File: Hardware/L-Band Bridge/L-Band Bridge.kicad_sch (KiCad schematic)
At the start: 0 parts

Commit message: Updating L-Band Bridge Schematic
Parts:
- added C1, C2: 100pF, symbol Device:C_Small
- added C3: 100nF, symbol Device:C_Small
- added J1, J2: SMA, symbol Connector:Conn_Coaxial
- added L1: 220nH, symbol Device:L_Small
- added R1: 8.25, symbol Device:R_Small_US
- added R2: 143, symbol Device:R_Small_US
- added U1: ADP-2-20+, RF_Mini-Circuits:Mini-Circuits_CD636_LandPatternPL-035, symbol _tim-RF:ADP-2-20+
- added U2, U3: ADL5904, Package_CSP:LFCSP-16-1EP_3x3mm_P0.5mm_EP1.6x1.6mm, symbol RF:ADL5904
- added U4, U5: GALI-52, Package_TO_SOT_SMD:SOT-89-3, symbol RF_Amplifier:GALI-52
- added U6: HMC472ALP4E, symbol _tim-RF:HMC472ALP4E
- added U7: ADE-17H+, RF_Mini-Circuits:Mini-Circuits_CD542_LandPatternPL-052, symbol _tim-RF:ADE-17H+
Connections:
- new net: U3.11 (GND), U3.17 (GND)
- new net: U3.5 (VPOS), U3.7 (VPOS)
- new net: U7.1 (GND), U7.4 (GND), U7.5 (GND)
- new net: U2.11 (GND), U2.17 (GND)
- new net: U2.5 (VPOS), U2.7 (VPOS)
- new net GND: J1.2 (Ext), U1.6 (GND), U6.1 (GND), U6.12 (GND), U6.14 (GND), U6.16 (GND), U6.17 (GND), U6.18 (GND), U6.25 (GND), U6.3 (GND), U6.5 (GND)
- new net RF_IN: J1.1 (In), U1.1 (SUM)
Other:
- note added: "ADE-17H+ Mixer (MOUSER)"
- note added: "ADP-2-20+ Power Divider"
- note added: "GALI-52+ AMP"
- note added: "HMC472ALP4 6-bit digital control attenuator"
- note added: "MAPS-010163-TR0500 1.4-2.4 GHz Phase Shifter"

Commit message: Updates to L-Band Bridge
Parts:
- removed U2, U3: ADL5904, Package_CSP:LFCSP-16-1EP_3x3mm_P0.5mm_EP1.6x1.6mm, symbol RF:ADL5904
- added C10, C11, C8, C9: 330pF, symbol Device:C_Small
- added C12, C13, C14, C4, C5: 100pF, symbol Device:C_Small
- added C15, C16, C20, C6, C7: 100nF, symbol Device:C_Small
- added C18, C19: 10nF, symbol Device:C_Small
- added J3: SMA, symbol Connector:Conn_Coaxial
- added L2: 220nH, symbol Device:L_Small
- added R3: 143, symbol Device:R_Small_US
- added R4: 8.25, symbol Device:R_Small_US
- added R5: 60.4, symbol Device:R_Small_US
- added R6: 2k, symbol Device:R_Small_US
- added R7: 3.74k, symbol Device:R_Small_US
- added R8: 1.5k, symbol Device:R_Small_US
- added R9: 270, symbol Device:R_Small_US
- added U10, U9: DBTC-17-5LX+, symbol _tim-RF:DBTC-17-5LX+
- added U2: ~, symbol _tim-RF:ADL5906
- added U8: ~, symbol _tim-RF:MAPS-010163-TR0500
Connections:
- net +12V: now also C3.2, R1.2, C6.2, R4.1
- net GND: now also C3.1, J2.2 (Ext), U4.2 (GND), U5.2 (GND), U7.1 (GND), U7.4 (GND), U7.5 (GND), C10.1, C11.1, C13.1, C14.2, C15.2, C16.1, C19.2, C20.2, C6.1, C7.2, C8.1, C9.1, J3.2 (Ext), R5.1, R6.1, R9.2, U10.2 (GND), U2.17 (GND), U2.4 (GND), U2.9 (GND), U8.10 (GND), U8.11 (GND), U8.12 (GND), U8.13 (GND), U8.15 (GND), U8.16 (GND), U8.2 (P/S), U8.25 (GND), U8.3 (GND), U8.4 (GND), U8.6 (GND), U8.7 (GND), U8.8 (GND), U8.9 (GND), U9.2 (GND)
- net at R1.1: now also R2.1
- net at U7.3 (RF): now also U10.4 (OUT)
- net at U7.6 (LO): now also C5.2
- net at U4.1: now also C1.2
- net at U4.3: now also C2.1, L1.2
- net at U6.10 (ACG5): now also C9.2
- net at U6.11 (ACG6): now also C10.2
- net at U6.13 (ACG7): now also C11.2
- net at U6.15 (RF2): now also C1.1
- net ATTEN_D0: now reaches U6.19 (V1)
- net +5V: now reaches U6.2 (Vdd)
- net +5V: now also C13.2, C14.1, C15.1, C16.2, C7.1, U2.10 (VPOS2), U2.3 (VPOS1), U8.18 (VCC)
- net ATTEN_D1: now reaches U6.20 (V2)
- net ATTEN_D2: now reaches U6.21 (V3)
- net ATTEN_D3: now reaches U6.22 (V4)
- net ATTEN_D4: now reaches U6.23 (V5)
- net ATTEN_D5: now reaches U6.24 (V6)
- net at U6.4 (RF1): now also C12.2
- net at U6.6 (ACG1): now also U6.7 (ACG2), U6.8 (ACG3), U6.9 (ACG4), C8.2
- net at L1.1: now also R2.2
- net at U5.1: now also C4.2
- net at U5.3: now also C5.1, L2.1
- net at U1.3 (PORT1): now also C12.1
- net at U1.4 (PORT2): now also U8.5 (RF_IN)
- net TX_OUT: now reaches J2.1 (In)
- net TX_OUT: now also U9.4 (OUT)
- net at C2.2: now also U9.3 (IN)
- net RF_IN renamed SYNTH_IN
- new net: R7.1, R8.2, U2.11 (VREF)
- new net: R6.2, R7.2, U2.12 (VTGT)
- new net: C19.1, U2.15 (RFIN-)
- new net: C4.1, U8.14 (RF_OUT)
- new net: R8.1, R9.1, U2.1 (TADJ)
- new net: C20.1, U2.5 (CRMS)
- new net: C18.1, U2.14 (RFIN+)
- new net: R3.2, R4.2
- new net: U2.13 (NIC), U2.16 (NIC), U2.2 (NIC)
- new net: L2.2, R3.1
- new net -5V: U8.1 (VEE)
- new net PHASE_D0: U8.24 (D1_SER_IN)
- new net PHASE_D1: U8.23 (D2_CLK)
- new net PHASE_D2: U8.22 (D3_LE)
- new net PHASE_D3: U8.21 (D4)
- new net PHASE_D4: U8.20 (D5)
- new net PHASE_D5: U8.19 (D6)
- new net PHASE_SER_OUT: U8.17 (SER_OUT)
- new net RX_IN: J3.1 (In), U10.3 (IN)
- new net RX_MON: U10.1 (CPLD)
- new net TX_MON: C18.2, R5.2, U9.1 (CPLD)
- new net TX_MON_VOUT: U2.6 (VRMS), U2.7 (VSET)
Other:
- note added: "+12V Input"
- note added: "DC-DC Converter 12V to +5V and -5V RP-1205D OR PDQE10-Q24-D5-D"
- note added: "Directional Coupler DBTC-17-5LX+"
- note added: "L-Band Transmitter/Receiver"
- note added: "P/S LOW => Parallel Mode"
- moved on the sheet: C1, C2, C3, J1, J2, L1, R1, R2, U1, U4, U5, U6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

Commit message: Updates to L-Band Bridge
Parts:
- added C17, C21: 3.9nF, symbol Device:C_Small
- added C22: 6.8nF, symbol Device:C_Small
- added C23, C24, C25, C26, C27, C28, C31, C33, C34: 100nF, symbol Device:C_Small
- added C29, C30, C32, C35, C41: 100pF, symbol Device:C_Small
- added C36: 100uF, symbol Device:C_Polarized_Small
- added C37, C38: 10uF, symbol Device:C_Small
- added C39, C40: 330pF, symbol Device:C_Small
- added L3, L4: 10uH, symbol Device:L_Small
- added PS1: PDQE10-Q24-D5-D, symbol _tim-DC_DC:PDQE10-Q24-D5-D
- added Q1: MMBT3904, Package_TO_SOT_THT:TO-92_Inline, symbol Transistor_BJT:MMBT3904
- added R10: 82k, symbol Device:R_Small_US
- added R11, R12, R23: 10k, symbol Device:R_Small_US
- added R13: 220, symbol Device:R_Small_US
- added R14: 60.4, symbol Device:R_Small_US
- added R15, R24: 100k, symbol Device:R_Small_US
- added R16: 50, symbol Device:R_Small_US
- added R17, R22: 2k, symbol Device:R_Small_US
- added R18: 18k, symbol Device:R_Small_US
- added R19: 3.74k, symbol Device:R_Small_US
- added R20: 1.5k, symbol Device:R_Small_US
- added R21: 270, symbol Device:R_Small_US
- added U11: ~, symbol _tim-RF:ADL5906
- added U3: LM358, symbol Amplifier_Operational:LM358
- C18, C19: value 10nF -> 100pF
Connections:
- net +12V: now also C28.2, C36.1, PS1.2 (VIN), R10.1, R12.1, R24.1, U3.8 (V+)
- net +5V: now also C31.1, C32.2, C34.2, C35.1, C37.2, C40.2, PS1.3 (+VOUT), U11.10 (VPOS2), U11.3 (VPOS1)
- net -5V: now also C38.1, C39.1, PS1.5 (-VOUT)
- net GND: now also C18.2, C17.2, C21.2, C22.2, C24.1, C26.1, C28.1, C30.2, C31.2, C32.1, C33.2, C34.1, C35.2, C36.2, C37.1, C38.2, C39.2, C40.1, C41.1, PS1.1 (GND), PS1.4 (0V), R11.2, R13.2, R14.1, R15.2, R21.2, R22.1, U11.17 (GND), U11.4 (GND), U11.9 (GND), U3.4 (V-); no longer C19.2
- net RX_MON: now also C19.1, R14.2
- net TX_MON: now also C29.1; no longer C18.2
- net 2.3V: now reaches R7.1, R8.2, U2.11 (VREF)
- net 2.3V: now also R19.1, R20.2, U11.11 (VREF)
- net at U2.15 (RFIN-): now also C18.1; no longer C19.1
- net IF: now reaches U7.2 (IF)
- net IF: now also C17.1, L3.1
- net at U2.14 (RFIN+): now also C29.2; no longer C18.1
- new net: C41.2, R23.1, U3.5 (+)
- new net: C26.2, R17.1
- new net: C33.1, U11.5 (CRMS)
- new net: C23.2, Q1.1 (B), R10.2, R11.1
- new net: R16.1, U3.6 (-), U3.7
- new net: C22.1, L3.2, L4.1
- new net: R18.1, R23.2, U3.1
- new net: C25.2, R15.1, R24.2, U3.3 (+)
- new net: C24.2, Q1.2 (E), R13.1
- new net: C30.1, U11.15 (RFIN-)
- new net: C19.2, U11.14 (RFIN+)
- new net: R17.2, R18.2, U3.2 (-)
- new net: C27.1, R16.2
- new net: R19.2, R22.2, U11.12 (VTGT)
- new net: R20.1, R21.1, U11.1 (TADJ)
- new net: U11.13 (NIC), U11.16 (NIC), U11.2 (NIC)
- new net IF_AMP_OUT: C25.1, Q1.3 (C), R12.2
- new net IF_LPF_OUT: C21.1, C23.1, L4.2
- new net IF_OUT: C27.2
- new net RX_MON_VOUT: U11.6 (VRMS), U11.7 (VSET)
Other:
- note added: "0.35V VTADJ Recommended for 10 MHz to 2.14 GHz"
- moved on the sheet: C13, C14, C15, C16, C20, R5, R6, R7, R8, R9, U2

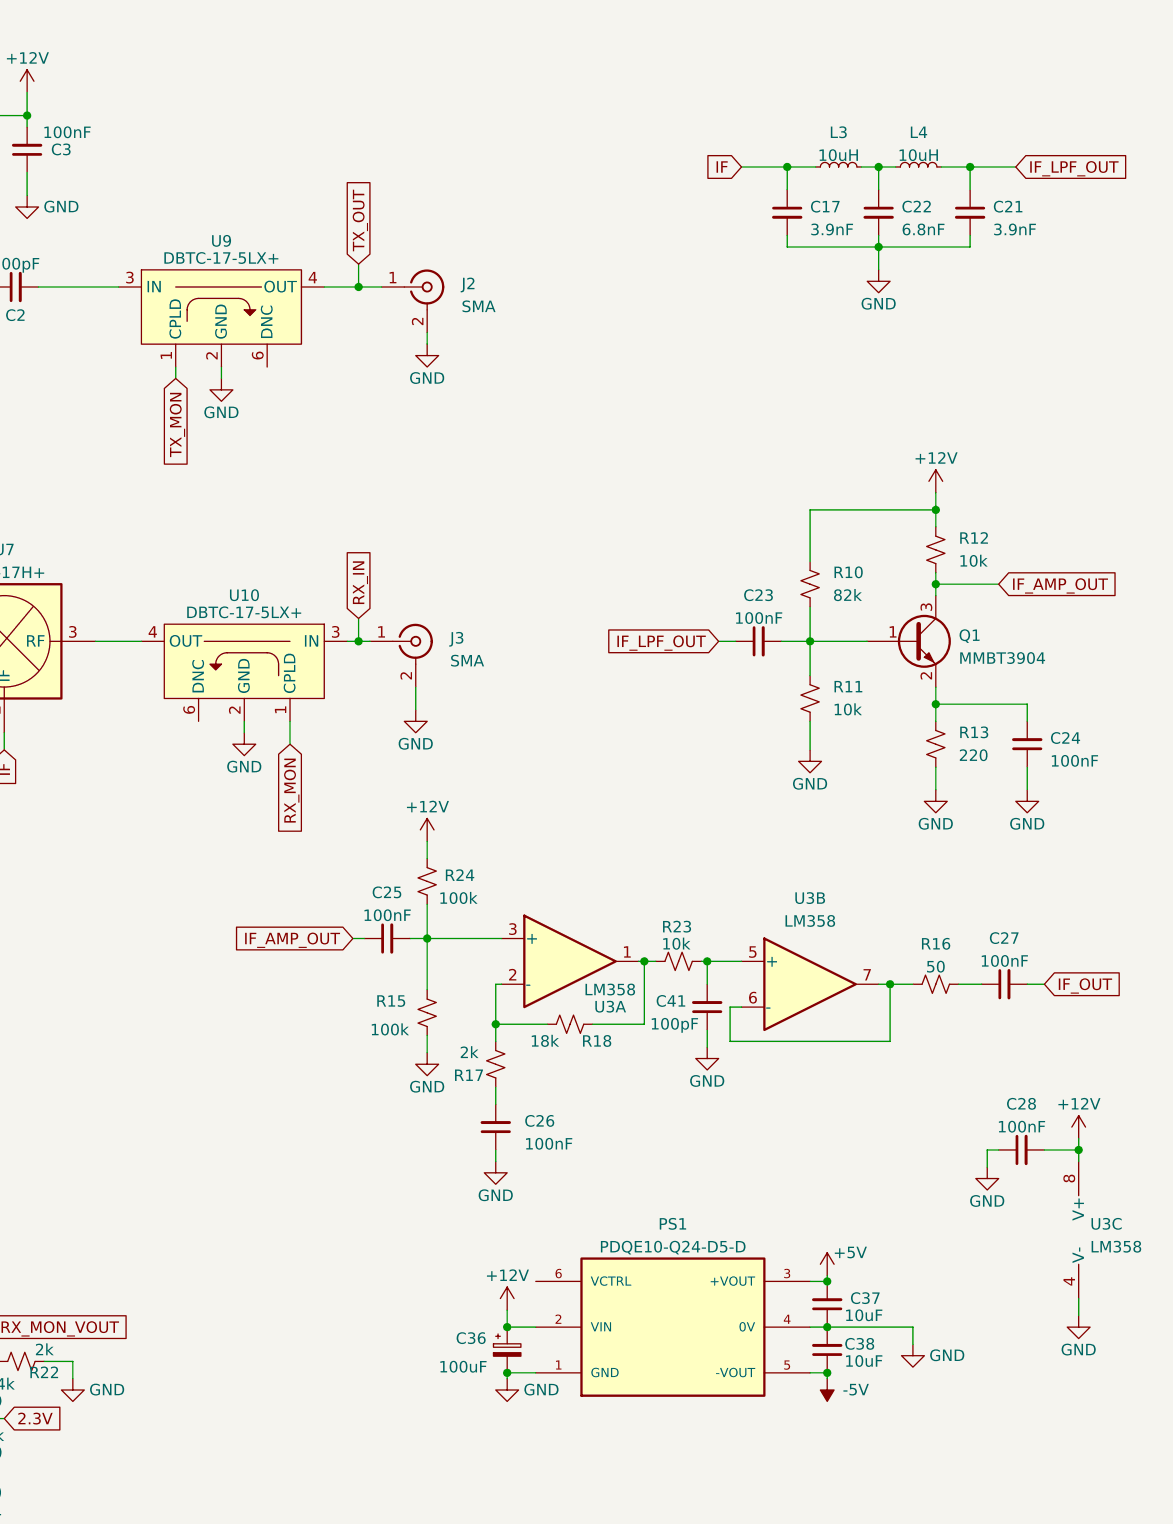
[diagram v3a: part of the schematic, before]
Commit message: L-Band Bridge Schematic Updates
Assigning footprints
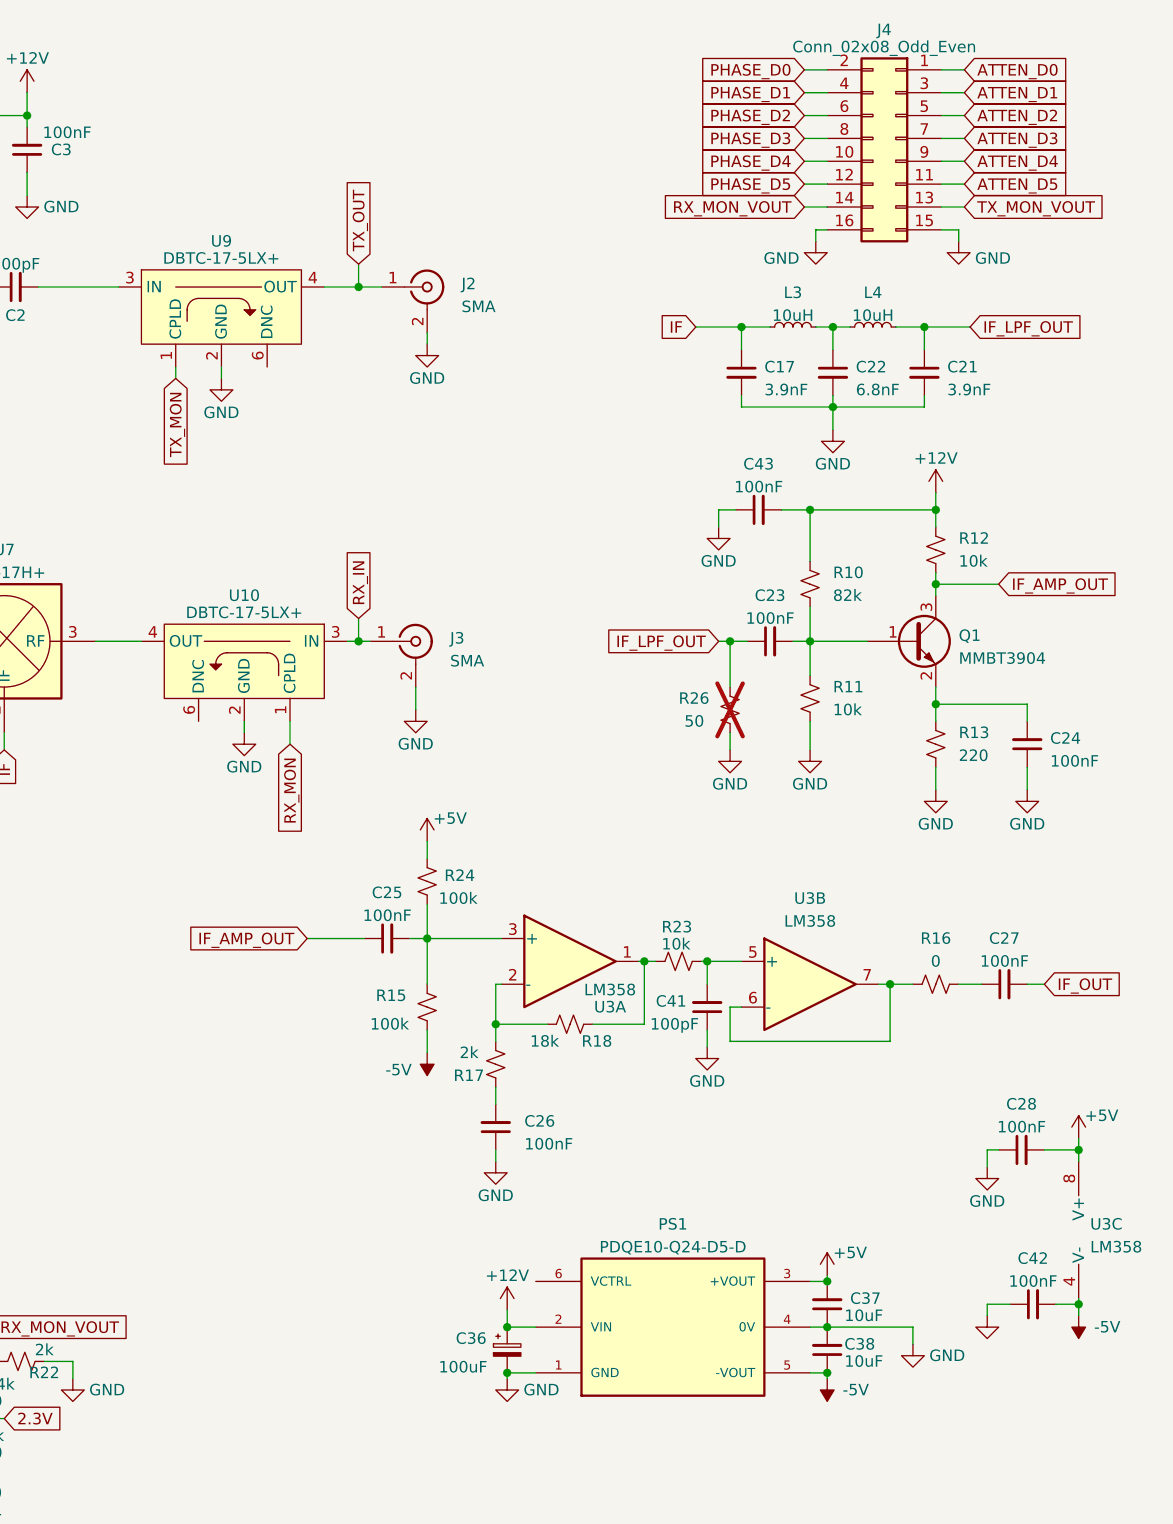
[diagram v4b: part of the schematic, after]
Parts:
- added C42, C43: 100nF, Capacitor_SMD:C_0402_1005Metric, symbol Device:C_Small
- added J4: Conn_02x08_Odd_Even, Connector_PinHeader_2.54mm:PinHeader_2x08_P2.54mm_Vertical, symbol Connector_Generic:Conn_02x08_Odd_Even
- added R26: 50, Capacitor_SMD:C_0603_1608Metric, symbol Device:R_Small_US
- C1, C10, C11, C12, C13, C14, C15, C16, C17, C18, C19, C2, C20, C21, C22, C23, C24, C25, C26, C27, C28, C29, C3, C30, C31, C32, C33, C34, C35, C39, C4, C40, C41, C5, C6, C7, C8, C9, R17, R18, R19, R20, R21, R22, R23, R24: footprint (none) -> Capacitor_SMD:C_0402_1005Metric
- J1, J2, J3: footprint (none) -> Connector_Coaxial:SMA_Amphenol_132291_Vertical
- R1, R4: footprint (none) -> Resistor_SMD:R_1206_3216Metric
- R10, R11, R12, R13, R14, R15, R6, R7, R8, R9: footprint (none) -> Resistor_SMD:R_0402_1005Metric
- R16: value 50 -> 0; footprint (none) -> Capacitor_SMD:C_0402_1005Metric
- R2, R3: footprint (none) -> Resistor_SMD:R_2010_5025Metric
- R5: footprint (none) -> Resistor_SMD:R_0603_1608Metric
- U3: footprint (none) -> Package_SO:MSOP-8_3x3mm_P0.65mm
- U6: footprint (none) -> Package_DFN_QFN:QFN-24-1EP_4x4mm_P0.5mm_EP2.7x2.7mm_ThermalVias
- U8: footprint (none) -> Package_DFN_QFN:QFN-24-1EP_4x4mm_P0.5mm_EP2.8x2.8mm_ThermalVias
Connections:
- net +12V: now also C43.2; no longer C28.2, R24.1, U3.8 (V+)
- net +5V: now also C28.2, R24.1, U3.8 (V+)
- net -5V: now also R15.2, U3.4 (V-), C42.2
- net ATTEN_D0: now also J4.1 (Pin_1)
- net ATTEN_D1: now also J4.3 (Pin_3)
- net ATTEN_D2: now also J4.5 (Pin_5)
- net ATTEN_D3: now also J4.7 (Pin_7)
- net ATTEN_D4: now also J4.9 (Pin_9)
- net ATTEN_D5: now also J4.11 (Pin_11)
- net GND: now also C42.1, C43.1, J4.15 (Pin_15), J4.16 (Pin_16), R26.2; no longer R15.2, U3.4 (V-)
- net IF_LPF_OUT: now also R26.1
- net PHASE_D0: now also J4.2 (Pin_2)
- net PHASE_D1: now also J4.4 (Pin_4)
- net PHASE_D2: now also J4.6 (Pin_6)
- net PHASE_D3: now also J4.8 (Pin_8)
- net PHASE_D4: now also J4.10 (Pin_10)
- net PHASE_D5: now also J4.12 (Pin_12)
- net RX_MON_VOUT: now also J4.14 (Pin_14)
- net TX_MON_VOUT: now also J4.13 (Pin_13)
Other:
- moved on the sheet: C17, C21, C22, C23, L3, L4, R15
